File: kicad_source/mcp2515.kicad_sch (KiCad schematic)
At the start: 14 parts, among them CN4 SM04B-GHS-TB, CN5 SM04B-GHS-TB, U8 MCP2515T-I/SO, U9 SN65HVD230, Y1 X322516MLB4SI

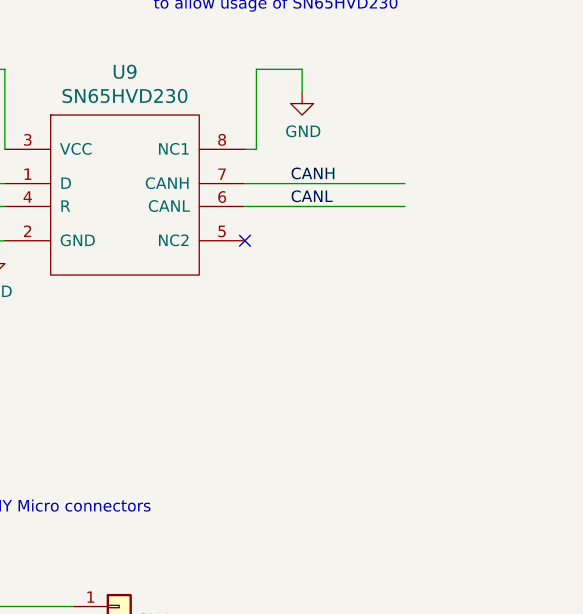
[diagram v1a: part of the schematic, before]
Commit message: removed C12, added CAN protection, updated schematic
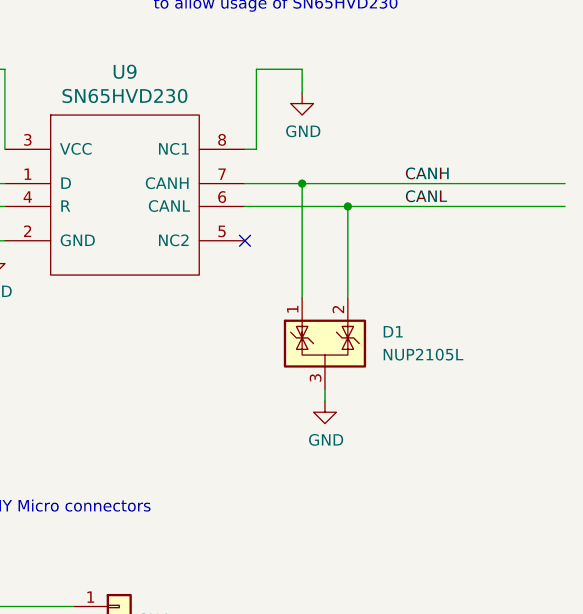
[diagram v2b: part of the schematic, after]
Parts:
- added D1: NUP2105L, Package_TO_SOT_SMD:SOT-23, symbol Power_Protection:NUP2105L
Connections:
- net CANH: now also D1.1 (K)
- net CANL: now also D1.2 (K)
- net GND: now also D1.3 (A)
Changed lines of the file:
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@@
   (junction (at 80.01 45.72) (diameter 0) (color 0 0 0 0)
   )
+  (junction (at 248.92 58.42) (diameter 0) (color 0 0 0 0)
+  )
   (junction (at 162.56 43.18) (diameter 0) (color 0 0 0 0)
+  )
+  (junction (at 243.84 55.88) (diameter 0) (color 0 0 0 0)
   )
   (junction (at 198.12 43.18) (diameter 0) (color 0 0 0 0)
@@
     (stroke (width 0) (type default) (color 0 0 0 0))
   )
+  (wire (pts (xy 237.49 58.42) (xy 248.92 58.42))
+    (stroke (width 0) (type default) (color 0 0 0 0))
+  )
   (wire (pts (xy 162.56 50.8) (xy 162.56 49.53))
     (stroke (width 0) (type default) (color 0 0 0 0))
@@
     (stroke (width 0) (type default) (color 0 0 0 0))
   )
+  (wire (pts (xy 248.92 58.42) (xy 273.05 58.42))
+    (stroke (width 0) (type default) (color 0 0 0 0))
+  )
   (wire (pts (xy 80.01 45.72) (xy 113.03 45.72))
     (stroke (width 0) (type default) (color 0 0 0 0))
@@
     (stroke (width 0) (type default) (color 0 0 0 0))
   )
+  (wire (pts (xy 237.49 55.88) (xy 243.84 55.88))
+    (stroke (width 0) (type default) (color 0 0 0 0))
+  )
   (wire (pts (xy 91.44 66.04) (xy 113.03 66.04))
     (stroke (width 0) (type default) (color 0 0 0 0))
@@
     (stroke (width 0) (type default) (color 0 0 0 0))
   )
-  (wire (pts (xy 255.27 58.42) (xy 237.49 58.42))
-    (stroke (width 0) (type default) (color 0 0 0 0))
-  )
   (wire (pts (xy 231.14 140.97) (xy 223.52 140.97))
     (stroke (width 0) (type default) (color 0 0 0 0))
@@
     (stroke (width 0) (type default) (color 0 0 0 0))
   )
+  (wire (pts (xy 248.92 58.42) (xy 248.92 68.58))
+    (stroke (width 0) (type default) (color 0 0 0 0))
+  )
   (wire (pts (xy 238.76 43.18) (xy 243.84 43.18))
     (stroke (width 0) (type default) (color 0 0 0 0))
@@
     (stroke (width 0) (type default) (color 0 0 0 0))
   )
-  (wire (pts (xy 255.27 55.88) (xy 237.49 55.88))
-    (stroke (width 0) (type default) (color 0 0 0 0))
-  )
   (wire (pts (xy 140.97 66.04) (xy 163.83 66.04))
     (stroke (width 0) (type default) (color 0 0 0 0))
@@
     (stroke (width 0) (type default) (color 0 0 0 0))
   )
+  (wire (pts (xy 243.84 55.88) (xy 273.05 55.88))
+    (stroke (width 0) (type default) (color 0 0 0 0))
+  )
+  (wire (pts (xy 246.38 78.74) (xy 246.38 80.01))
+    (stroke (width 0) (type default) (color 0 0 0 0))
+  )
   (wire (pts (xy 163.83 81.28) (xy 166.37 81.28))
     (stroke (width 0) (type default) (color 0 0 0 0))
@@
     (stroke (width 0) (type default) (color 0 0 0 0))
   )
+  (wire (pts (xy 243.84 55.88) (xy 243.84 68.58))
+    (stroke (width 0) (type default) (color 0 0 0 0))
+  )
   (wire (pts (xy 163.83 66.04) (xy 163.83 81.28))
     (stroke (width 0) (type default) (color 0 0 0 0))
@@
     (effects (font (size 1.27 1.27)) (justify left bottom))
   )
-  (label "CANH" (at 242.57 55.88 0)
+  (label "CANH" (at 255.27 55.88 0)
     (effects (font (size 1.27 1.27)) (justify left bottom))
   )
@@
     (effects (font (size 1.27 1.27)) (justify left bottom))
   )
-  (label "CANL" (at 242.57 58.42 0)
+  (label "CANL" (at 255.27 58.42 0)
     (effects (font (size 1.27 1.27)) (justify left bottom))
   )
@@
     (pin "1")
   )
+  (symbol (lib_id "OpenCyphalPicoBase-rescue:GND-power-supply") (at 246.38 80.01 0) (unit 1)
+    (in_bom yes) (on_board yes)
+    (property "Reference" "#PWR020" (id 0) (at 246.38 86.36 0)
+      (effects (font (size 1.27 1.27)) hide)
+    )
+    (property "Value" "GND" (id 1) (at 246.507 84.4042 0))
+    (property "Footprint" "" (id 2) (at 246.38 80.01 0))
+    (property "Datasheet" "" (id 3) (at 246.38 80.01 0))
+    (pin "1")
+  )
+  (symbol (lib_id "Power_Protection:NUP2105L") (at 246.38 73.66 0) (unit 1)
+    (in_bom yes) (on_board yes) (fields_autoplaced)
+    (property "Reference" "D1" (id 0) (at 252.73 72.3899 0)
+      (effects (font (size 1.27 1.27)) (justify left))
+    )
+    (property "Value" "NUP2105L" (id 1) (at 252.73 74.9299 0)
+      (effects (font (size 1.27 1.27)) (justify left))
+    )
+    (property "Footprint" "Package_TO_SOT_SMD:SOT-23" (id 2) (at 252.095 74.93 0)
+      (effects (font (size 1.27 1.27)) (justify left) hide)
+    )
+    (property "Datasheet" "http://www.onsemi.com/pub_link/Collateral/NUP2105L-D.PDF" (id 3) (at 249.555 70.485 0)
+      (effects (font (size 1.27 1.27)) hide)
+    )
+    (pin "3")
+    (pin "1")
+    (pin "2")
+  )
   (symbol (lib_id "Device:Fuse_Small") (at 204.47 156.21 0) (unit 1)

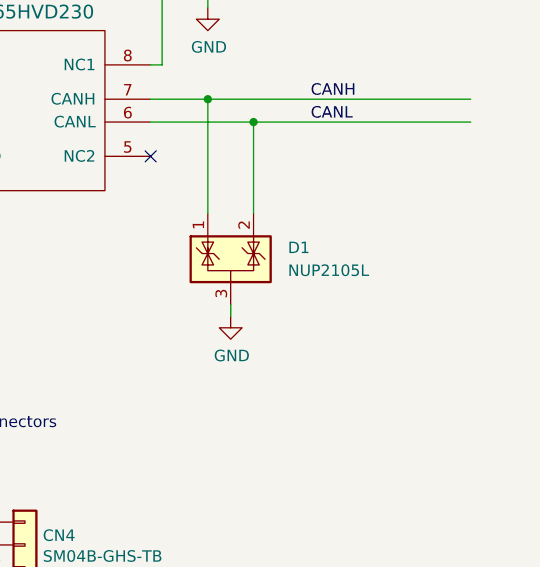
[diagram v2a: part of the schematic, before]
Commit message: added qwiic logo, made DRC
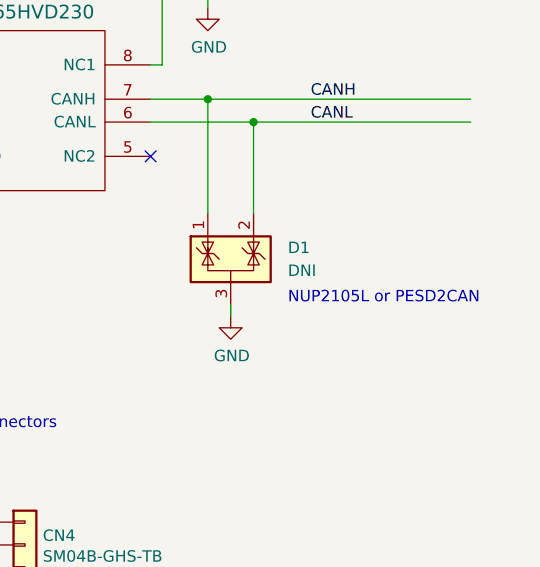
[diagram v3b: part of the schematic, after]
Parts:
- C7, C8: now left out of the parts list
- D1: value NUP2105L -> DNI; now left out of the parts list
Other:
- note added: "NUP2105L or PESD2CAN"
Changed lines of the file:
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@@
   (title_block
     (title "OpenCyphalPicoBase")
-    (date "2023-08-08")
+    (date "2023-08-09")
     (rev "0.3")
     (company "generationmake")
@@
   )
   (text "16MHz" (at 181.61 82.55 0)
+    (effects (font (size 1.27 1.27)) (justify left bottom))
+  )
+  (text "NUP2105L or PESD2CAN" (at 252.73 78.74 0)
     (effects (font (size 1.27 1.27)) (justify left bottom))
   )
@@
   )
   (symbol (lib_id "Device:C_Small") (at 176.53 85.09 0) (unit 1)
-    (in_bom yes) (on_board yes)
+    (in_bom no) (on_board yes)
     (property "Reference" "C8" (id 0) (at 178.8668 83.9216 0)
       (effects (font (size 1.27 1.27)) (justify left))
@@
   )
   (symbol (lib_id "Device:C_Small") (at 163.83 85.09 0) (mirror y) (unit 1)
-    (in_bom yes) (on_board yes)
+    (in_bom no) (on_board yes)
     (property "Reference" "C7" (id 0) (at 161.4932 83.9216 0)
       (effects (font (size 1.27 1.27)) (justify left))
@@
   )
   (symbol (lib_id "Power_Protection:NUP2105L") (at 246.38 73.66 0) (unit 1)
-    (in_bom yes) (on_board yes) (fields_autoplaced)
+    (in_bom no) (on_board yes) (fields_autoplaced)
     (property "Reference" "D1" (id 0) (at 252.73 72.3899 0)
       (effects (font (size 1.27 1.27)) (justify left))
     )
-    (property "Value" "NUP2105L" (id 1) (at 252.73 74.9299 0)
-      (effects (font (size 1.27 1.27)) (justify left))
-    )
+    (property "Value" "DNI" (id 1) (at 252.73 74.9299 0)
+      (effects (font (size 1.27 1.27)) (justify left))
+    )
